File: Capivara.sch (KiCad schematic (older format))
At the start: 63 parts, among them J1 COMM, J2 PROG, J3 INSTR, J4 GENERAL, J5 UART, U1 STM32F303CCTx, U2 AMS1117-3.3, U3 TL084, U4 MCP6002-xSN, U5 ADS1115IDGS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

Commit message: Mudanças Pezzi
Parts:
- added C19, C20: 10n, OPL_Capacitor:C0603, symbol Device:C
- added J6: DAC_OUT, Connector_PinHeader_2.54mm:PinHeader_1x03_P2.54mm_Vertical, symbol Connector:Conn_01x03_Male
- added R24, R25, R26, R27: 1k, OPL_Resistor:R0603, symbol Device:R
- added U6: MCP6002-xSN, OPL_Integrated_Circuit:SOIC8-1.27-5X4MM, symbol Amplifier_Operational:MCP6002-xSN
- C13: footprint OPL_Resistor:R0603 -> OPL_Resistor:R0805
- R10, R9: value 220 -> 470
- R11, R12, R13, R15, R6, R7: value 33k -> 68k
- R14: value 1k2 -> 1k
- R20, R21, R22, R23: value 220 -> 120
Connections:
- net +3.3VADC: now also R24.1, U6.8 (V+)
- net A7_OP4: now also U1.26 (PB13); no longer U1.14 (PA4)
- net A8_OP3: now also U1.18 (PB0); no longer U1.15 (PA5)
- net GND: now also C19.2, C20.2, J6.1 (Pin_1), R25.2, U6.4 (V-); no longer R6.2, U3.12 (+), U3.13 (-)
- net LED0: now also U1.25 (PB12); no longer U1.26 (PB13)
- net at U3.14: now also R6.2, U3.13 (-)
- new net: R24.2, R25.1, U3.12 (+)
- new net: C19.1, R26.1, U6.5 (+)
- new net: J6.2 (Pin_2), U6.6 (-), U6.7
- new net: J6.3 (Pin_3), U6.1, U6.2 (-)
- new net: C20.1, R27.1, U6.3 (+)
- new net DAC1_OUT1: R26.2, U1.14 (PA4)
- new net DAC1_OUT2: R27.2, U1.15 (PA5)
- no-connect marks 23 -> 20
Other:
- note added: "15.9kHz low-pass\n"
- note added: "Gain = 69\nHigher gain is possible using the internal PGA (up to 1104)"
- note added: "Vref"
- note added: "We use 5V as Seeed \ndoesn't stock quad RRO opamps"
- note removed: "Gain = 55\nHigher gain is possible using the internal PGA (up to 880)"
- note removed: "We use 5V as Seeed doesn't stock quad RRO opamps"
- moved on the sheet: U3D

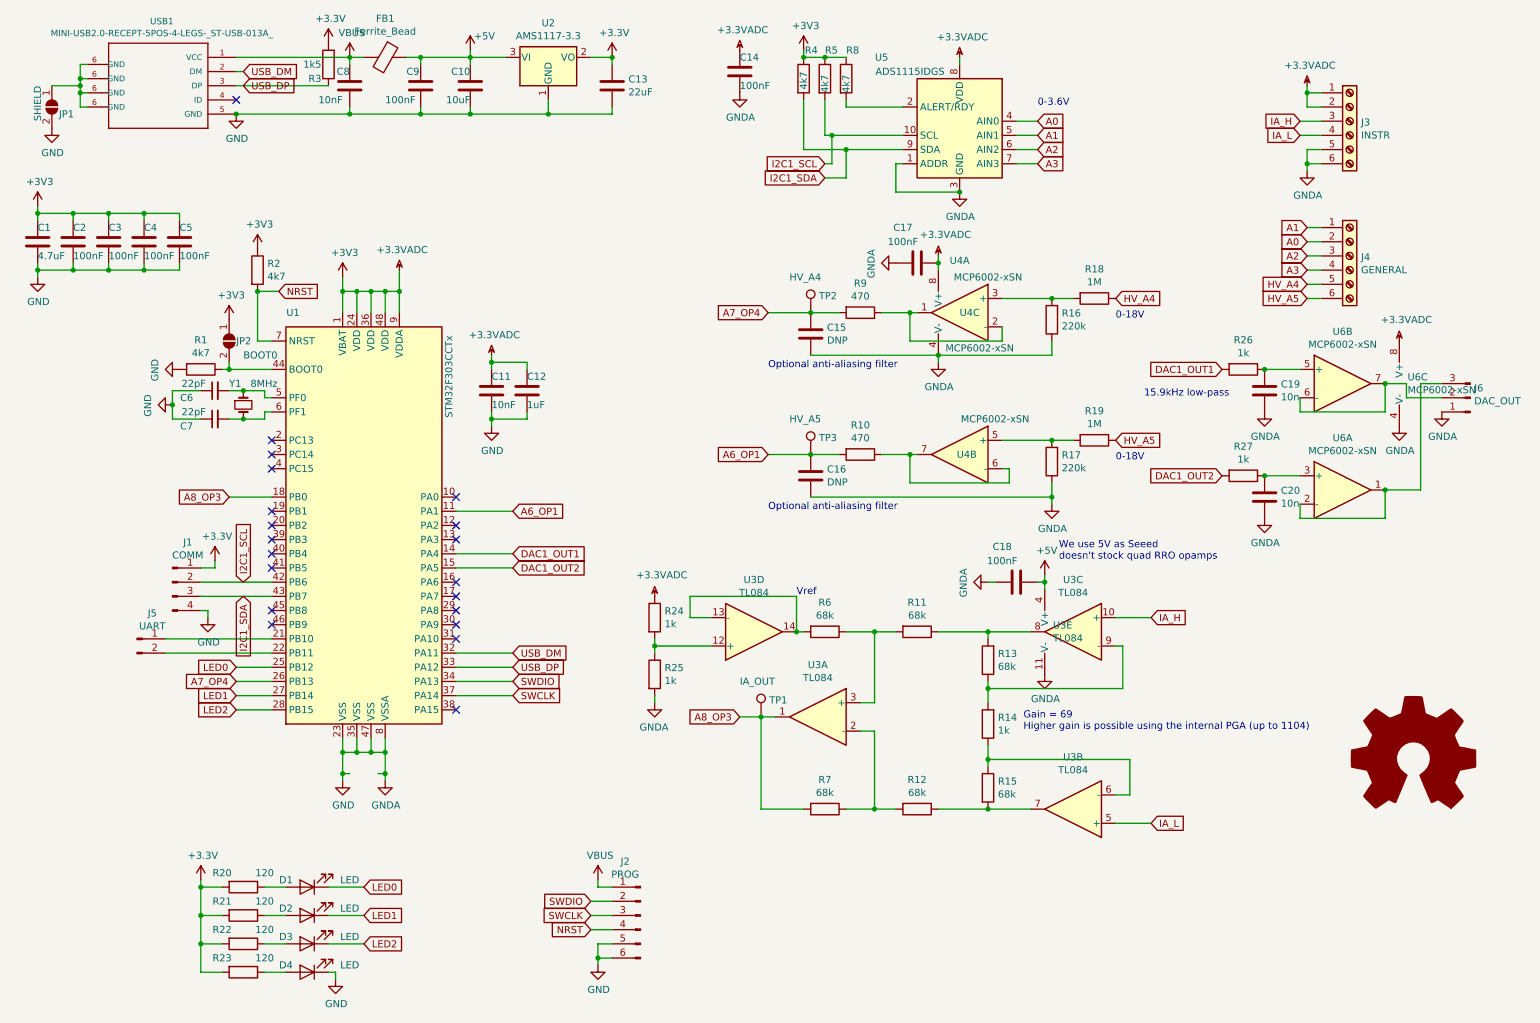
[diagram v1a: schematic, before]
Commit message: Usar INA ao invés de InsOp discreto
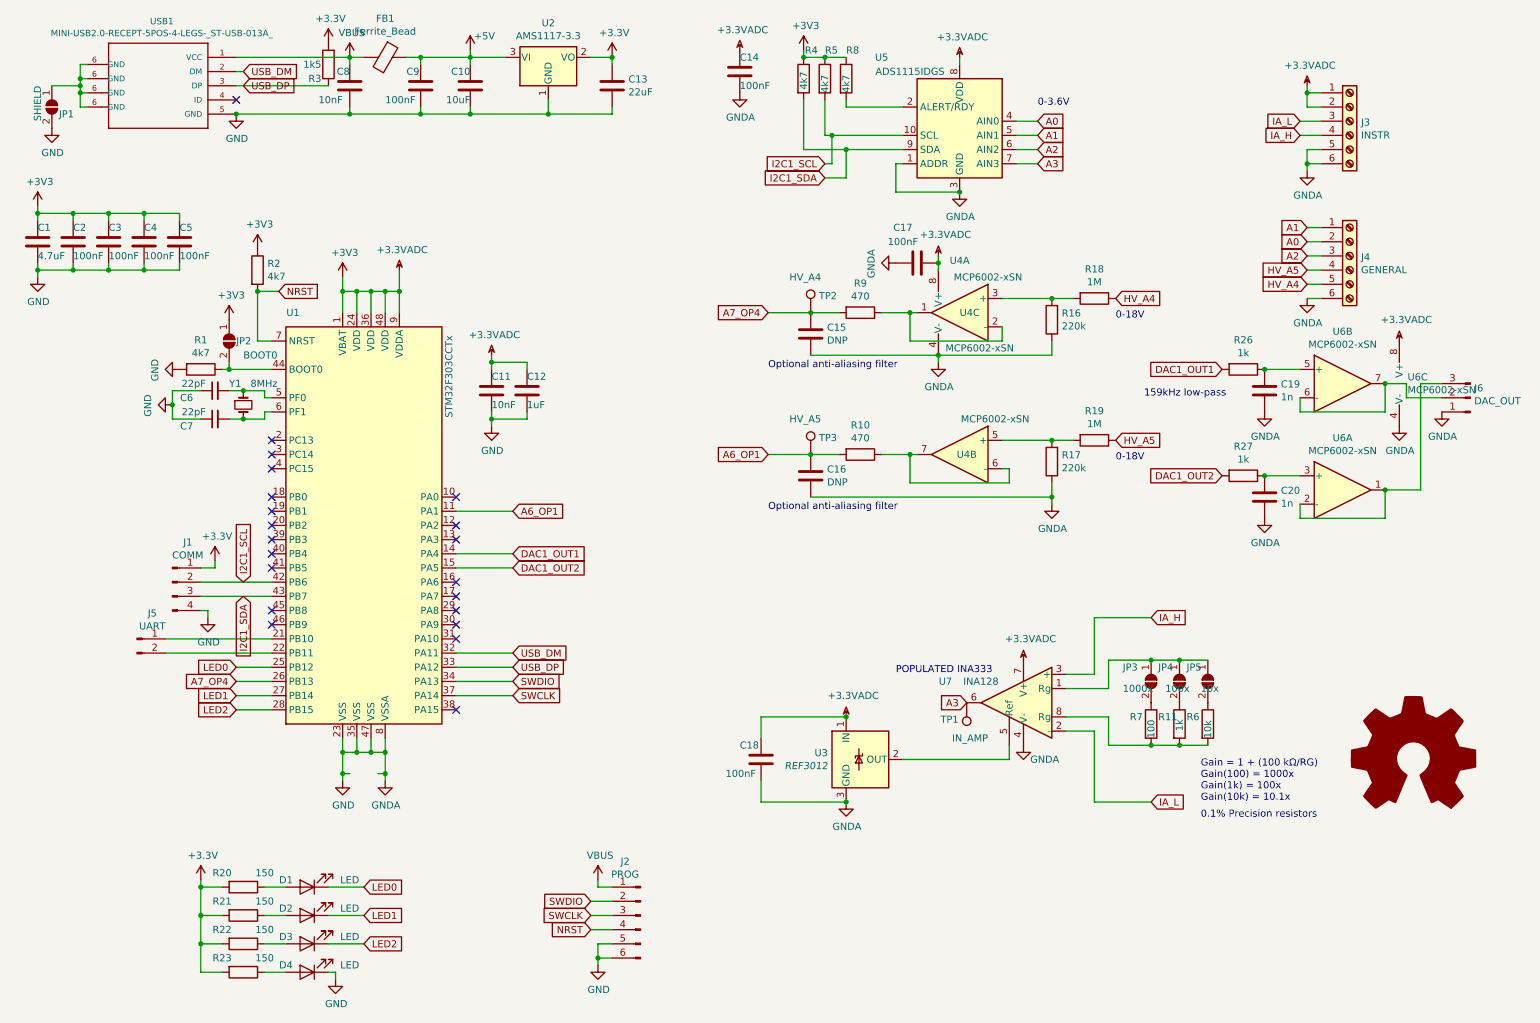
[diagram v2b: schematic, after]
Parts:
- removed R12, R13, R15: 68k, OPL_Resistor:R0603, symbol Device:R
- removed R14, R24, R25: 1k, OPL_Resistor:R0603, symbol Device:R
- removed U3: TL084, Package_SO:SOIC-14_3.9x8.7mm_P1.27mm, symbol Amplifier_Operational:TL084
- added JP3: 1000x, Jumper:SolderJumper-2_P1.3mm_Open_RoundedPad1.0x1.5mm, symbol Jumper:SolderJumper_2_Open
- added JP4: 100x, Jumper:SolderJumper-2_P1.3mm_Open_RoundedPad1.0x1.5mm, symbol Jumper:SolderJumper_2_Open
- added JP5: 10x, Jumper:SolderJumper-2_P1.3mm_Open_RoundedPad1.0x1.5mm, symbol Jumper:SolderJumper_2_Open
- added U3: REF3012, Package_TO_SOT_SMD:SOT-23, symbol Reference_Voltage:REF3012
- added U7: INA128, Package_SO:VSSOP-8_3.0x3.0mm_P0.65mm, symbol Amplifier_Instrumentation:INA128
- C19, C20: value 10n -> 1n
- R11: value 68k -> 1k
- R20, R21, R22, R23: value 120 -> 150
- R6: value 68k -> 10k
- R7: value 68k -> 100
- TP1: value IA_OUT -> IN_AMP
- U6: footprint (none) -> OPL_Integrated_Circuit:SOIC8-1.27-5X4MM
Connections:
- net +3.3VADC: now also C18.1, U3.1 (IN), U7.7 (V+)
- net +5V: no longer C18.1
- net A3: now also TP1.1, U7.6; no longer J4.4 (Pin_4)
- net GND: now also J4.6 (Pin_6), U3.3 (GND), U7.4 (V-)
- net HV_A5: now also J4.4 (Pin_4); no longer J4.6 (Pin_6)
- net IA_H: now also J3.4 (Pin_4), U7.3 (+); no longer J3.3 (Pin_3)
- net IA_L: now also J3.3 (Pin_3), U7.2 (-); no longer J3.4 (Pin_4)
- net at R11.1: now also JP4.2 (B)
- net at R11.2: now also R6.2, R7.2, U7.8 (Rg); no longer R6.1
- net at R7.1: now also JP3.2 (B)
- removed net A8_OP3: R7.2, TP1.1, U1.18 (PB0)
- new net: JP3.1 (A), JP4.1 (A), JP5.1 (A), U7.1 (Rg)
- new net: U3.2 (OUT), U7.5 (Ref)
- new net: JP5.2 (B), R6.1
- no-connect marks 20 -> 21
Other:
- note added: "0.1% Precision resistors\n\n"
- note added: "159kHz low-pass\n"
- note added: "Gain = 1 + (100 kΩ/RG)\nGain(100) = 1000x\nGain(1k) = 100x\nGain(10k) = 10.1x"
- note added: "POPULATED INA333\n"
- note removed: "15.9kHz low-pass\n"
- note removed: "Gain = 69\nHigher gain is possible using the internal PGA (up to 1104)"
- note removed: "Vref"
- note removed: "We use 5V as Seeed \ndoesn't stock quad RRO opamps"
